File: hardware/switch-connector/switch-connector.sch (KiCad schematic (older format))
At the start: 10 parts, among them P1 12V, P2 Relay OFF (NC), P3 Sensing, P4 Coil, P5 Relay On enable (NO), P6 NO, P7 Common, SW1 NC: Off, SW2 NO: On, SW3 NC: E-Stop

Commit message: o make hierarchical sheet.
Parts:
- removed P1: 12V, Pin_Headers:Pin_Header_Straight_1x02, symbol CONN_01X02
- removed P2: Relay OFF (NC), Pin_Headers:Pin_Header_Straight_1x02, symbol CONN_01X02
- removed P3: Sensing, Pin_Headers:Pin_Header_Straight_1x04, symbol CONN_01X04
- removed P4: Coil, Pin_Headers:Pin_Header_Straight_1x01, symbol CONN_01X01
- removed P5: Relay On enable (NO), Pin_Headers:Pin_Header_Straight_1x02, symbol CONN_01X02
- removed P6: NO, Pin_Headers:Pin_Header_Straight_1x01, symbol CONN_01X01
- removed P7: Common, Pin_Headers:Pin_Header_Straight_1x01, symbol CONN_01X01
- removed SW1: NC: Off, Pin_Headers:Pin_Header_Straight_1x02, symbol SW_PUSH
- removed SW2: NO: On, Pin_Headers:Pin_Header_Straight_1x02, symbol SW_PUSH
- removed SW3: NC: E-Stop, Pin_Headers:Pin_Header_Straight_1x02, symbol SW_PUSH
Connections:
- wire segments 23 -> 0
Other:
- note added: "Black"
- note added: "Red"
- note added: "Yellow"
- note removed: "NO"
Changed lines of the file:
@@
 LIBS:contrib
 LIBS:valves
+LIBS:relays
 LIBS:switch-connector-cache
 EELAYER 25 0
@@
 $Descr A4 11693 8268
 encoding utf-8
-Sheet 1 1
+Sheet 1 2
 Title ""
 Date ""
@@
 Comment4 ""
 $EndDescr
-$Comp
-L SW_PUSH SW1
-U 1 1 57D0AB9F
-P 2650 2600
-F 0 "SW1" H 2800 2710 50  0000 C CNN
-F 1 "NC: Off" H 2650 2520 50  0000 C CNN
-F 2 "Pin_Headers:Pin_Header_Straight_1x02" H 2650 2600 50  0001 C CNN
-F 3 "" H 2650 2600 50  0000 C CNN
-	1    2650 2600
-	1    0    0    -1
-$EndComp
-$Comp
-L CONN_01X02 P1
-U 1 1 57D0AC23
-P 1150 2750
-F 0 "P1" H 1150 2900 50  0000 C CNN
-F 1 "12V" V 1250 2750 50  0000 C CNN
-F 2 "Pin_Headers:Pin_Header_Straight_1x02" H 1150 2750 50  0001 C CNN
-F 3 "" H 1150 2750 50  0000 C CNN
-	1    1150 2750
-	-1   0    0    1
-$EndComp
-Wire Notes Line
-	3700 3400 3700 3550
-Wire Notes Line
-	3650 3550 3750 3550
-Wire Notes Line
-	3650 3550 3650 3700
-Wire Notes Line
-	3650 3700 3750 3700
-Wire Notes Line
-	3750 3700 3750 3550
-Wire Notes Line
-	3700 3700 3700 3750
-Wire Notes Line
-	3700 3750 3900 3750
-Wire Notes Line
-	3850 3750 3850 3700
-Text Notes 3800 3650 0    39   ~ 0
-NO
-Wire Wire Line
-	1350 3000 3700 3000
-Wire Wire Line
-	3250 2900 3800 2900
-Wire Wire Line
-	3800 2900 3800 3000
-Wire Wire Line
-	4050 2950 3900 2950
-Wire Wire Line
-	3900 2950 3900 3000
-Wire Notes Line
-	3800 3400 3800 3550
-Wire Notes Line
-	3900 3750 3900 3400
-$Comp
-L SW_PUSH SW2
-U 1 1 57D0AC74
-P 3650 2600
-F 0 "SW2" H 3800 2710 50  0000 C CNN
-F 1 "NO: On" H 3650 2520 50  0000 C CNN
-F 2 "Pin_Headers:Pin_Header_Straight_1x02" H 3650 2600 50  0001 C CNN
-F 3 "" H 3650 2600 50  0000 C CNN
-	1    3650 2600
-	1    0    0    -1
-$EndComp
-Wire Wire Line
-	3100 2600 3350 2600
-Wire Wire Line
-	3250 2400 3250 2900
-Connection ~ 3250 2600
-$Comp
-L CONN_01X02 P5
-U 1 1 57D0B52B
-P 4000 2100
-F 0 "P5" H 4000 2250 50  0000 C CNN
-F 1 "Relay On enable (NO)" V 4100 1800 50  0000 C CNN
-F 2 "Pin_Headers:Pin_Header_Straight_1x02" H 4000 2100 50  0001 C CNN
-F 3 "" H 4000 2100 50  0000 C CNN
-	1    4000 2100
-	0    -1   -1   0
-$EndComp
-Wire Wire Line
-	3950 2300 3950 2600
-Wire Wire Line
-	4050 2300 4050 2950
-$Comp
-L CONN_01X02 P2
-U 1 1 57D0B59A
-P 3050 2100
-F 0 "P2" H 3050 2250 50  0000 C CNN
-F 1 "Relay OFF (NC)" V 3150 2250 50  0000 C CNN
-F 2 "Pin_Headers:Pin_Header_Straight_1x02" H 3050 2100 50  0001 C CNN
-F 3 "" H 3050 2100 50  0000 C CNN
-	1    3050 2100
-	0    -1   -1   0
-$EndComp
-Wire Wire Line
-	3000 2300 3000 2600
-Wire Wire Line
-	3000 2600 2950 2600
-Wire Wire Line
-	3100 2300 3100 2600
-Wire Wire Line
-	3250 2400 3400 2400
-Wire Wire Line
-	3400 2400 3400 2300
-Wire Wire Line
-	3600 2300 4050 2300
-Connection ~ 4050 2300
-Wire Wire Line
-	3500 2300 3500 2400
-Wire Wire Line
-	3500 2400 3950 2400
-Connection ~ 3950 2400
-$Comp
-L SW_PUSH SW3
-U 1 1 57D0C011
-P 1850 2600
-F 0 "SW3" H 2000 2710 50  0000 C CNN
-F 1 "NC: E-Stop" H 1850 2520 50  0000 C CNN
-F 2 "Pin_Headers:Pin_Header_Straight_1x02" H 1850 2600 50  0001 C CNN
-F 3 "" H 1850 2600 50  0000 C CNN
-	1    1850 2600
-	1    0    0    -1
-$EndComp
-$Comp
-L CONN_01X04 P3
-U 1 1 57D0C0C3
-P 3450 2100
-F 0 "P3" H 3450 2350 50  0000 C CNN
-F 1 "Sensing" V 3550 2100 50  0000 C CNN
-F 2 "Pin_Headers:Pin_Header_Straight_1x04" H 3450 2100 50  0001 C CNN
-F 3 "" H 3450 2100 50  0000 C CNN
-	1    3450 2100
-	0    -1   -1   0
-$EndComp
-Wire Wire Line
-	2150 2600 2350 2600
-Wire Wire Line
-	3300 2300 2300 2300
-Wire Wire Line
-	2300 2300 2300 2600
-Connection ~ 2300 2600
-Wire Wire Line
-	1550 2600 1350 2600
-Wire Wire Line
-	1350 2600 1350 2700
-Wire Wire Line
-	1350 2800 1350 3000
-$Comp
-L CONN_01X01 P4
-U 1 1 57D0BFC6
-P 3700 3200
-F 0 "P4" H 3700 3300 50  0000 C CNN
-F 1 "Coil" V 3850 3100 50  0000 C CNN
-F 2 "Pin_Headers:Pin_Header_Straight_1x01" H 3700 3200 50  0001 C CNN
-F 3 "" H 3700 3200 50  0000 C CNN
-	1    3700 3200
-	0    1    1    0
-$EndComp
-$Comp
-L CONN_01X01 P6
-U 1 1 57D0BFFC
-P 3800 3200
-F 0 "P6" H 3800 3300 50  0000 C CNN
-F 1 "NO" V 3950 3200 50  0000 C CNN
-F 2 "Pin_Headers:Pin_Header_Straight_1x01" H 3800 3200 50  0001 C CNN
-F 3 "" H 3800 3200 50  0000 C CNN
-	1    3800 3200
-	0    1    1    0
-$EndComp
-$Comp
-L CONN_01X01 P7
-U 1 1 57D0C02A
-P 3900 3200
-F 0 "P7" H 3900 3300 50  0000 C CNN
-F 1 "Common" V 4050 3350 50  0000 C CNN
-F 2 "Pin_Headers:Pin_Header_Straight_1x01" H 3900 3200 50  0001 C CNN
-F 3 "" H 3900 3200 50  0000 C CNN
-	1    3900 3200
-	0    1    1    0
-$EndComp
+$Sheet
+S 3450 3200 1700 850
+U 58AB5D07
+F0 "switch-box" 60
+F1 "switch-box.sch" 60
+F2 "Trigger" O R 5150 3550 60
+F3 "Sustain" O R 5150 3700 60
+F4 "CoilGnd" O R 5150 3850 60
+F5 "Sense-E-Stop" O L 3450 3400 60
+F6 "Sense-Off" O L 3450 3550 60
+F7 "Sense-On" O L 3450 3700 60
+F8 "Sense-Powered" O L 3450 3850 60
+$EndSheet
+Text Notes 5200 3500 0    60   ~ 0
+Yellow
+Text Notes 5200 3650 0    60   ~ 0
+Red
+Text Notes 5200 3800 0    60   ~ 0
+Black
 $EndSCHEMATC

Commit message: o Add relay to the toplevel schematic
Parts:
- added RL?: Omron-LY4NJ, symbol Omron-LY4NJ
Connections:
- net labels added: Phase_1, Phase_2
- wire segments 0 -> 11
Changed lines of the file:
@@
 LIBS:valves
 LIBS:relays
+LIBS:parts
 LIBS:switch-connector-cache
 EELAYER 25 0
@@
 F8 "Sense-Powered" O L 3450 3850 60
 $EndSheet
-Text Notes 5200 3500 0    60   ~ 0
+Text Notes 5200 3650 0    60   ~ 0
 Yellow
-Text Notes 5200 3650 0    60   ~ 0
+Text Notes 5200 3800 0    60   ~ 0
 Red
-Text Notes 5200 3800 0    60   ~ 0
+Text Notes 5200 3950 0    60   ~ 0
 Black
+$Comp
+L Omron-LY4NJ RL?
+U 1 1 58ABB826
+P 6150 4500
+F 0 "RL?" H 5720 4546 50  0000 R CNN
+F 1 "Omron-LY4NJ" H 5720 4455 50  0000 R CNN
+F 2 "" H 6150 4500 50  0000 C CNN
+F 3 "" H 6150 4500 50  0000 C CNN
+	1    6150 4500
+	1    0    0    -1
+$EndComp
+Wire Wire Line
+	5600 4800 6350 4800
+Wire Wire Line
+	5600 4800 5600 3550
+Wire Wire Line
+	5600 3550 5150 3550
+Connection ~ 5950 4800
+Wire Wire Line
+	5150 3700 6250 3700
+Wire Wire Line
+	6250 3700 6250 4200
+Wire Wire Line
+	5150 3850 5950 3850
+Wire Wire Line
+	5950 3850 5950 4200
+Wire Wire Line
+	7050 4200 7050 3800
+Wire Wire Line
+	7450 4200 7450 3800
+Wire Wire Line
+	7150 4800 7150 5100
+Wire Wire Line
+	7550 4800 7550 5100
+Text Label 7050 3850 1    60   ~ 0
+Phase_1
+Text Label 7450 3850 1    60   ~ 0
+Phase_2
 $EndSCHEMATC

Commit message: o clarifications in schematic
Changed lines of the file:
@@
 LIBS:relays
 LIBS:parts
+LIBS:switches
 LIBS:switch-connector-cache
 EELAYER 25 0
@@
 F6 "Sense-Off" O L 3450 3550 60
 F7 "Sense-On" O L 3450 3700 60
-F8 "Sense-Powered" O L 3450 3850 60
+F8 "Sense-Sustained" O L 3450 3850 60
 $EndSheet
 Text Notes 5200 3650 0    60   ~ 0

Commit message: Upgrade to new eeschema lib.
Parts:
- RL?: symbol Omron-LY4NJ -> parts:Omron-LY4NJ
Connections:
- wire segments 11 -> 12
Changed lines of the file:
@@
-EESchema Schematic File Version 2
-LIBS:power
-LIBS:device
-LIBS:transistors
-LIBS:conn
-LIBS:linear
-LIBS:regul
-LIBS:74xx
-LIBS:cmos4000
-LIBS:adc-dac
-LIBS:memory
-LIBS:xilinx
-LIBS:microcontrollers
-LIBS:dsp
-LIBS:microchip
-LIBS:analog_switches
-LIBS:motorola
-LIBS:texas
-LIBS:intel
-LIBS:audio
-LIBS:interface
-LIBS:digital-audio
-LIBS:philips
-LIBS:display
-LIBS:cypress
-LIBS:siliconi
-LIBS:opto
-LIBS:atmel
-LIBS:contrib
-LIBS:valves
-LIBS:relays
-LIBS:parts
-LIBS:switches
+EESchema Schematic File Version 4
 LIBS:switch-connector-cache
-EELAYER 25 0
+EELAYER 26 0
 EELAYER END
 $Descr A4 11693 8268
@@
 Black
 $Comp
-L Omron-LY4NJ RL?
+L parts:Omron-LY4NJ RL?
 U 1 1 58ABB826
 P 6150 4500
@@
 $EndComp
 Wire Wire Line
-	5600 4800 6350 4800
+	5600 4800 5950 4800
 Wire Wire Line
 	5600 4800 5600 3550
@@
 Text Label 7450 3850 1    60   ~ 0
 Phase_2
+Wire Wire Line
+	5950 4800 6350 4800
 $EndSCHEMATC

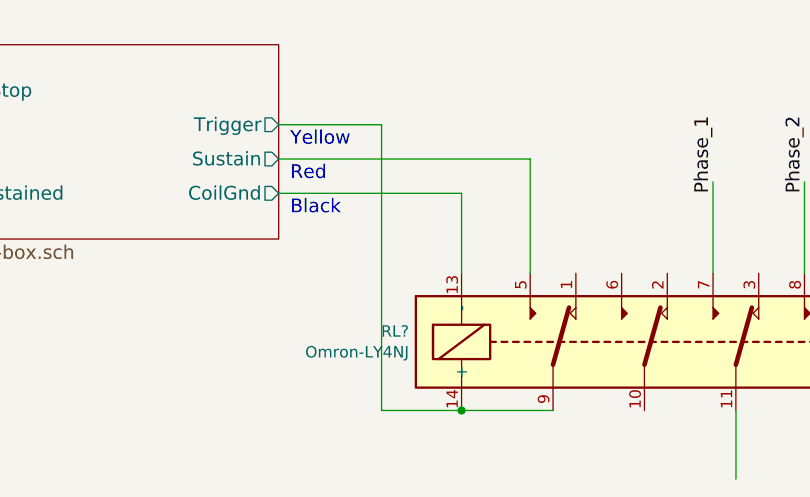
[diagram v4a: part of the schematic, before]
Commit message: A little more silkscreen to ease assembly.
Also:
o enough space for actual connectors for switches and sense outputs
o have inputs for every single switch ('eStop' and 'off' were sharing one)
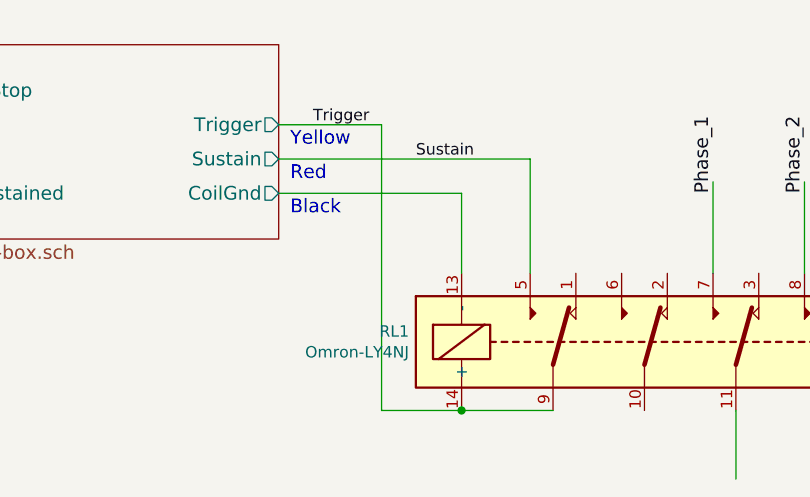
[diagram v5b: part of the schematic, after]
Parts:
- gave numbers to parts that had none: 1
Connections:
- net labels added: Sustain, Trigger
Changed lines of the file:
@@
 Black
 $Comp
-L parts:Omron-LY4NJ RL?
+L parts:Omron-LY4NJ RL1
 U 1 1 58ABB826
 P 6150 4500
-F 0 "RL?" H 5720 4546 50  0000 R CNN
+F 0 "RL1" H 5720 4546 50  0000 R CNN
 F 1 "Omron-LY4NJ" H 5720 4455 50  0000 R CNN
 F 2 "" H 6150 4500 50  0000 C CNN
@@
 Wire Wire Line
 	5950 4800 6350 4800
+Text Label 5750 3700 0    50   ~ 0
+Sustain
+Text Label 5300 3550 0    50   ~ 0
+Trigger
 $EndSCHEMATC

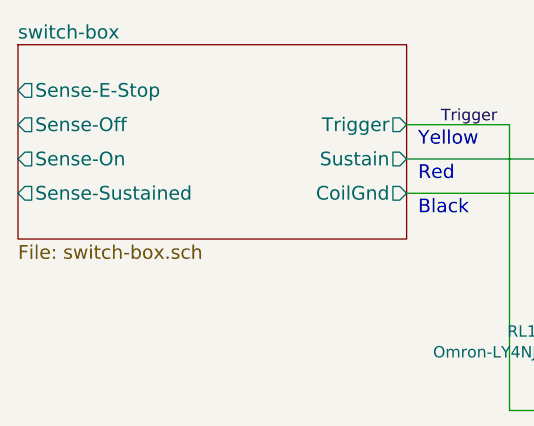
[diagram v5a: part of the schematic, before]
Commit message: Update schematic to refined design.
(PCB still needs to be adapted)
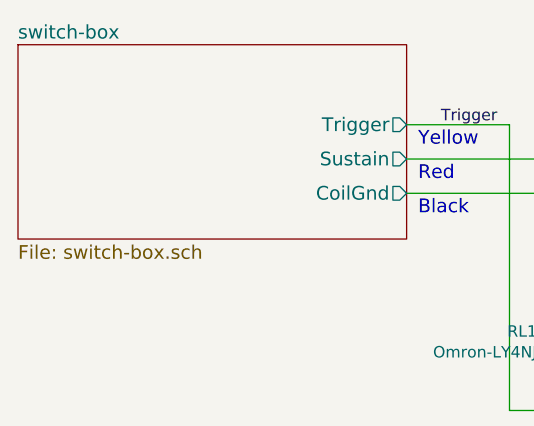
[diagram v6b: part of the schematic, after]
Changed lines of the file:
@@
 F3 "Sustain" O R 5150 3700 60
 F4 "CoilGnd" O R 5150 3850 60
-F5 "Sense-E-Stop" O L 3450 3400 60
-F6 "Sense-Off" O L 3450 3550 60
-F7 "Sense-On" O L 3450 3700 60
-F8 "Sense-Sustained" O L 3450 3850 60
 $EndSheet
 Text Notes 5200 3650 0    60   ~ 0
